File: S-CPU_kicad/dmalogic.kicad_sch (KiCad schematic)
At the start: 186 parts

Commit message: Schematics update.
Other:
- company: (none) -> Author: Regis Galland
- title: (none) -> SNES S-CPU Schematics 
- moved on the sheet: DBWG, DBZJ, DCBP, DMA?, EBSG, EBVQ, EBXE, EBYP, ECCU, ECEK, ECGN, ECGO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

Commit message: Schematics tidying in progress.
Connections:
- net wDBJW_wHASI_RST renamed wDBJW_wHASI_~{RST}
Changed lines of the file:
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@@
   (title_block
     (title "SNES S-CPU Schematics ")
-    (date "2023-06-14")
+    (date "2023-10-19")
     (rev "0.1")
     (company "Author: Regis Galland")
@@
     (effects (font (size 1.27 1.27)) (justify left))
   )
-  (hierarchical_label "wDBJW_wHASI_RST" (shape input) (at 93.345 63.5 180) (fields_autoplaced)
+  (hierarchical_label "wDBJW_wHASI_~{RST}" (shape input) (at 93.345 63.5 180) (fields_autoplaced)
     (effects (font (size 1.27 1.27)) (justify right))
   )
@@
     (effects (font (size 1.27 1.27)) (justify right))
   )
-  (hierarchical_label "wDBJW_wHASI_RST" (shape input) (at 601.345 253.365 180) (fields_autoplaced)
+  (hierarchical_label "wDBJW_wHASI_~{RST}" (shape input) (at 601.345 253.365 180) (fields_autoplaced)
     (effects (font (size 1.27 1.27)) (justify right))
   )

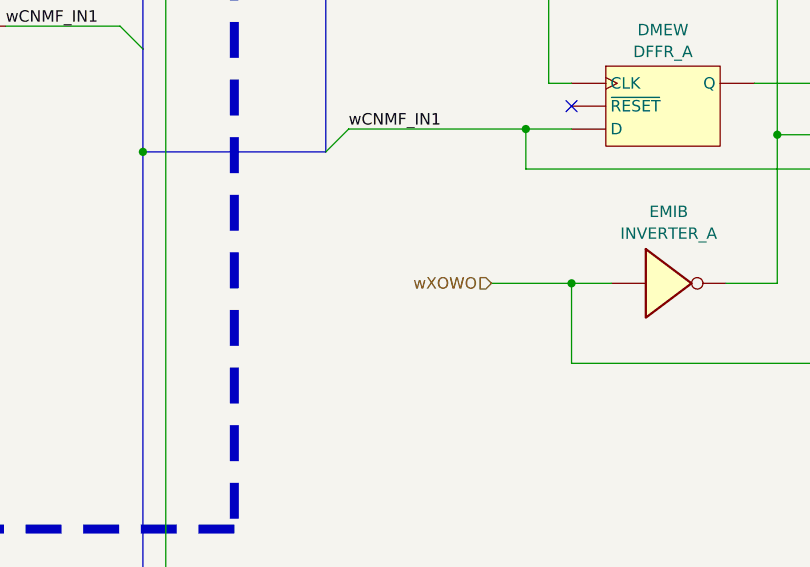
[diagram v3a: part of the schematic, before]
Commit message: DMA section update. Fixed gate related to INC/DEC and BORROW/CARRY FLAG
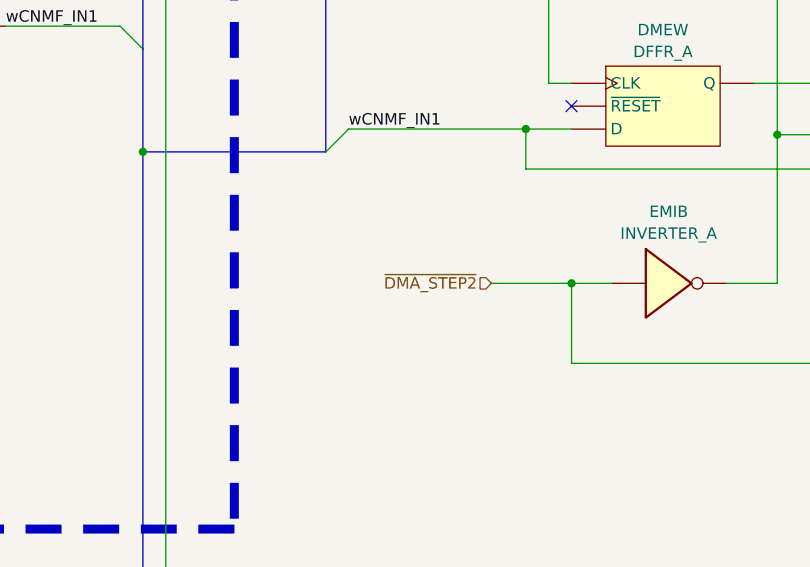
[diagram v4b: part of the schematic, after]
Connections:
- net wXOWO renamed ~{DMA_STEP2}
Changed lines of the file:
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@@
     (effects (font (size 1.27 1.27)) (justify right))
   )
-  (hierarchical_label "wXOWO" (shape input) (at 723.9 473.075 180) (fields_autoplaced)
+  (hierarchical_label "~{DMA_STEP2}" (shape input) (at 723.9 473.075 180) (fields_autoplaced)
     (effects (font (size 1.27 1.27)) (justify right))
   )

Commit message: General update a
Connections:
- net ~{GDMA_CHAN_RST} renamed ~{DMA_CHAN_RST}
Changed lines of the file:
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@@
     (effects (font (size 1.27 1.27)) (justify right))
   )
-  (hierarchical_label "~{GDMA_CHAN_RST}" (shape input) (at 254 44.45 180) (fields_autoplaced)
+  (hierarchical_label "~{DMA_CHAN_RST}" (shape input) (at 254 44.45 180) (fields_autoplaced)
     (effects (font (size 1.27 1.27)) (justify right))
   )
